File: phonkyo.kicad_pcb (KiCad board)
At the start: 2 copper layers, 65 x 30 mm, 39 parts, among them J1 GPIO, J2 LineOutJack, J4 RIJack, U1 CAT24C256, U2 PCM5102A, U3 XC6206P332MR

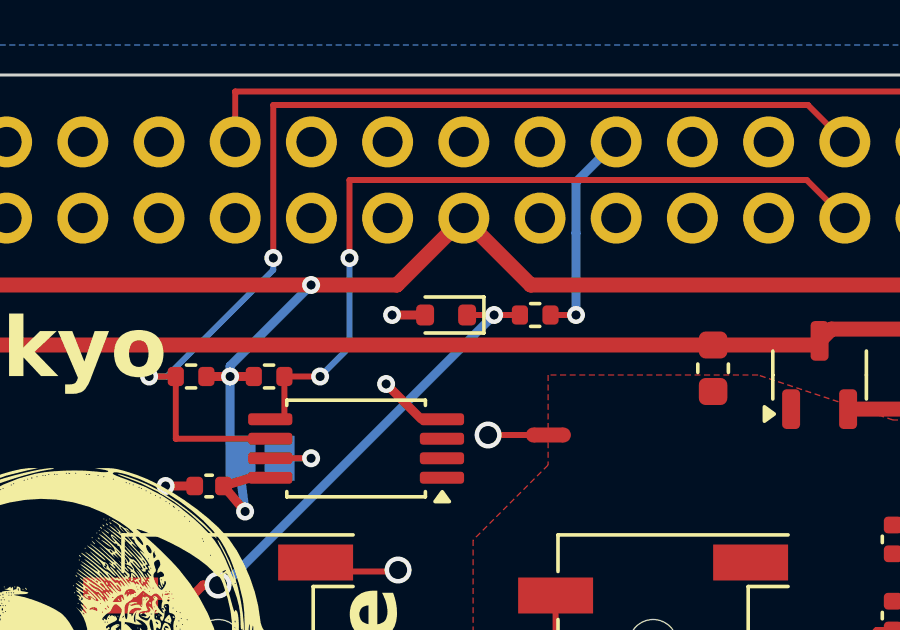
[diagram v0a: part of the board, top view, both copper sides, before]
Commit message: pcb: shift D1 so its silkscreen cathode bar clears the via
The SOD-523 outline's cathode bar landed on the ring of the jack-side
via, so the ink printed over the via and looked cramped. Move D1 and its
GND via 0.3 mm left. The bar now sits in clear board. DRC is unchanged
(0 unconnected, 0 parity). Production files are regenerated.
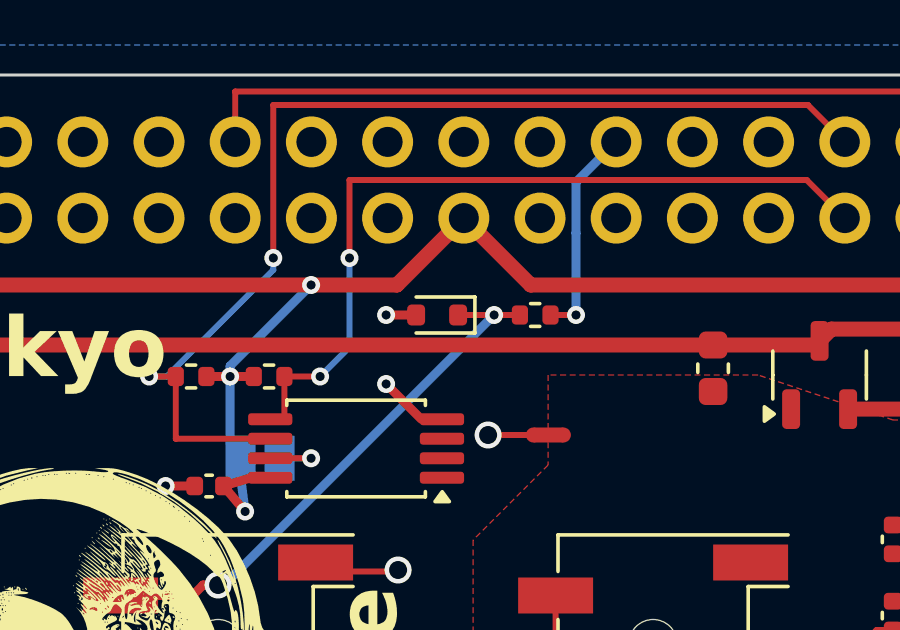
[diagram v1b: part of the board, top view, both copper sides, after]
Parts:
- moved D1 0.30 mm to (127.8, 78.0)
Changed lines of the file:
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@@
 				(font
 					(size 1.27 1.27)
+					(thickness 0.15)
 				)
 			)
@@
 	(footprint "Diode_SMD:D_SOD-523"
 		(layer "F.Cu")
-		(at 128.1 78 180)
+		(at 127.8 78 180)
 		(descr "http://www.diodes.com/datasheets/ap02001.pdf p.144")
 		(tags "Diode SOD523")
@@
 				(font
 					(size 1.27 1.27)
+					(thickness 0.15)
 				)
 			)
@@
 	)
 	(segment
-		(start 127.4 78)
-		(end 126.3 78)
+		(start 127.1 78)
+		(end 126.1 78)
 		(width 0.3)
 		(layer "F.Cu")
@@
 	)
 	(via
-		(at 126.3 78)
+		(at 126.1 78)
 		(size 0.6)
 		(drill 0.3)
@@
 	)
 	(segment
+		(start 131.58 78)
+		(end 132.43 78)
+		(width 0.2)
+		(layer "F.Cu")
+		(net "/GPIO25")
+	)
+	(via
+		(at 132.43 78)
+		(size 0.6)
+		(drill 0.3)
+		(layers "F.Cu" "B.Cu")
+		(net "/GPIO25")
+	)
+	(segment
+		(start 132.43 75.27)
+		(end 132.43 78)
+		(width 0.3)
+		(layer "B.Cu")
+		(net "/GPIO25")
+	)
+	(segment
+		(start 132.43 73.57)
+		(end 132.43 75.267057)
+		(width 0.3)
+		(layer "B.Cu")
+		(net "/GPIO25")
+	)
+	(segment
+		(start 133.77 72.23)
+		(end 132.43 73.57)
+		(width 0.3)
+		(layer "B.Cu")
+		(net "/GPIO25")
+	)
+	(segment
+		(start 119.65 87.35)
+		(end 117.25 87.35)
+		(width 0.3)
+		(layer "F.Cu")
+		(net "Net-(D1-K)")
+	)
+	(segment
+		(start 128.5 78)
+		(end 130.56 78)
+		(width 0.2)
+		(layer "F.Cu")
+		(net "Net-(D1-K)")
+	)
+	(segment
+		(start 120 87)
+		(end 119.65 87.35)
+		(width 0.3)
+		(layer "F.Cu")
+		(net "Net-(D1-K)")
+	)
+	(segment
+		(start 120.5 87)
+		(end 120 87)
+		(width 0.3)
+		(layer "F.Cu")
+		(net "Net-(D1-K)")
+	)
+	(via
+		(at 129.699999 78)
+		(size 0.6)
+		(drill 0.3)
+		(layers "F.Cu" "B.Cu")
+		(net "Net-(D1-K)")
+	)
+	(via
+		(at 120.5 87)
+		(size 0.9)
+		(drill 0.6)
+		(layers "F.Cu" "B.Cu")
+		(capping no)
+		(covering
+			(front no)
+			(back no)
+		)
+		(plugging
+			(front no)
+			(back no)
+		)
+		(filling no)
+		(net "Net-(D1-K)")
+	)
+	(segment
+		(start 120.697057 87)
+		(end 120.5 87)
+		(width 0.3)
+		(layer "B.Cu")
+		(net "Net-(D1-K)")
+	)
+	(segment
+		(start 120.7 87)
+		(end 129.699999 78)
+		(width 0.3)
+		(layer "B.Cu")
+		(net "Net-(D1-K)")
+	)
+	(segment
 		(start 141.39 72.23)
 		(end 140.16 71)
@@
 	)
 	(segment
-		(start 131.58 78)
-		(end 132.43 78)
-		(width 0.2)
-		(layer "F.Cu")
-		(net "/GPIO25")
-	)
-	(via
-		(at 132.43 78)
-		(size 0.6)
-		(drill 0.3)
-		(layers "F.Cu" "B.Cu")
-		(net "/GPIO25")
-	)
-	(segment
-		(start 132.43 75.27)
-		(end 132.43 78)
-		(width 0.3)
-		(layer "B.Cu")
-		(net "/GPIO25")
-	)
-	(segment
-		(start 132.43 73.57)
-		(end 132.43 75.267057)
-		(width 0.3)
-		(layer "B.Cu")
-		(net "/GPIO25")
-	)
-	(segment
-		(start 133.77 72.23)
-		(end 132.43 73.57)
-		(width 0.3)
-		(layer "B.Cu")
-		(net "/GPIO25")
-	)
-	(segment
 		(start 146.4 87.4)
 		(end 146 87)
@@
 		(net "Net-(JP1-A)")
 	)
-	(segment
-		(start 119.65 87.35)
-		(end 117.25 87.35)
-		(width 0.3)
-		(layer "F.Cu")
-		(net "Net-(D1-K)")
-	)
-	(segment
-		(start 128.8 78)
-		(end 130.56 78)
-		(width 0.2)
-		(layer "F.Cu")
-		(net "Net-(D1-K)")
-	)
-	(segment
-		(start 120 87)
-		(end 119.65 87.35)
-		(width 0.3)
-		(layer "F.Cu")
-		(net "Net-(D1-K)")
-	)
-	(segment
-		(start 120.5 87)
-		(end 120 87)
-		(width 0.3)
-		(layer "F.Cu")
-		(net "Net-(D1-K)")
-	)
-	(via
-		(at 129.699999 78)
-		(size 0.6)
-		(drill 0.3)
-		(layers "F.Cu" "B.Cu")
-		(net "Net-(D1-K)")
-	)
-	(via
-		(at 120.5 87)
-		(size 0.9)
-		(drill 0.6)
-		(layers "F.Cu" "B.Cu")
-		(capping no)
-		(covering
-			(front no)
-			(back no)
-		)
-		(plugging
-			(front no)
-			(back no)
-		)
-		(filling no)
-		(net "Net-(D1-K)")
-	)
-	(segment
-		(start 120.697057 87)
-		(end 120.5 87)
-		(width 0.3)
-		(layer "B.Cu")
-		(net "Net-(D1-K)")
-	)
-	(segment
-		(start 120.7 87)
-		(end 129.699999 78)
-		(width 0.3)
-		(layer "B.Cu")
-		(net "Net-(D1-K)")
-	)
 	(zone
